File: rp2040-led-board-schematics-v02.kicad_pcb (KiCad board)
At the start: 2 copper layers, 135.9 x 80 mm, 98 parts, among them IC1 UA78L05CDR, J1 GPIO, J10 LED1Terminal, J2 PWR_IN, J3 LED1Terminal, J4 LED1Terminal, J5 LED1Terminal, J6 LED1Terminal, J7 LED1Terminal, J8 LED1Terminal, J9 LED1Terminal, SW1 Button, SW2 PEC16-2115F-S0012, U1 Pico, U10 MAX485E, U2 ENC28J60, U3 MAX485E, U4 MAX485E, U5 MAX485E, U6 MAX485E, U7 MAX485E, U8 MAX485E, U9 MAX485E

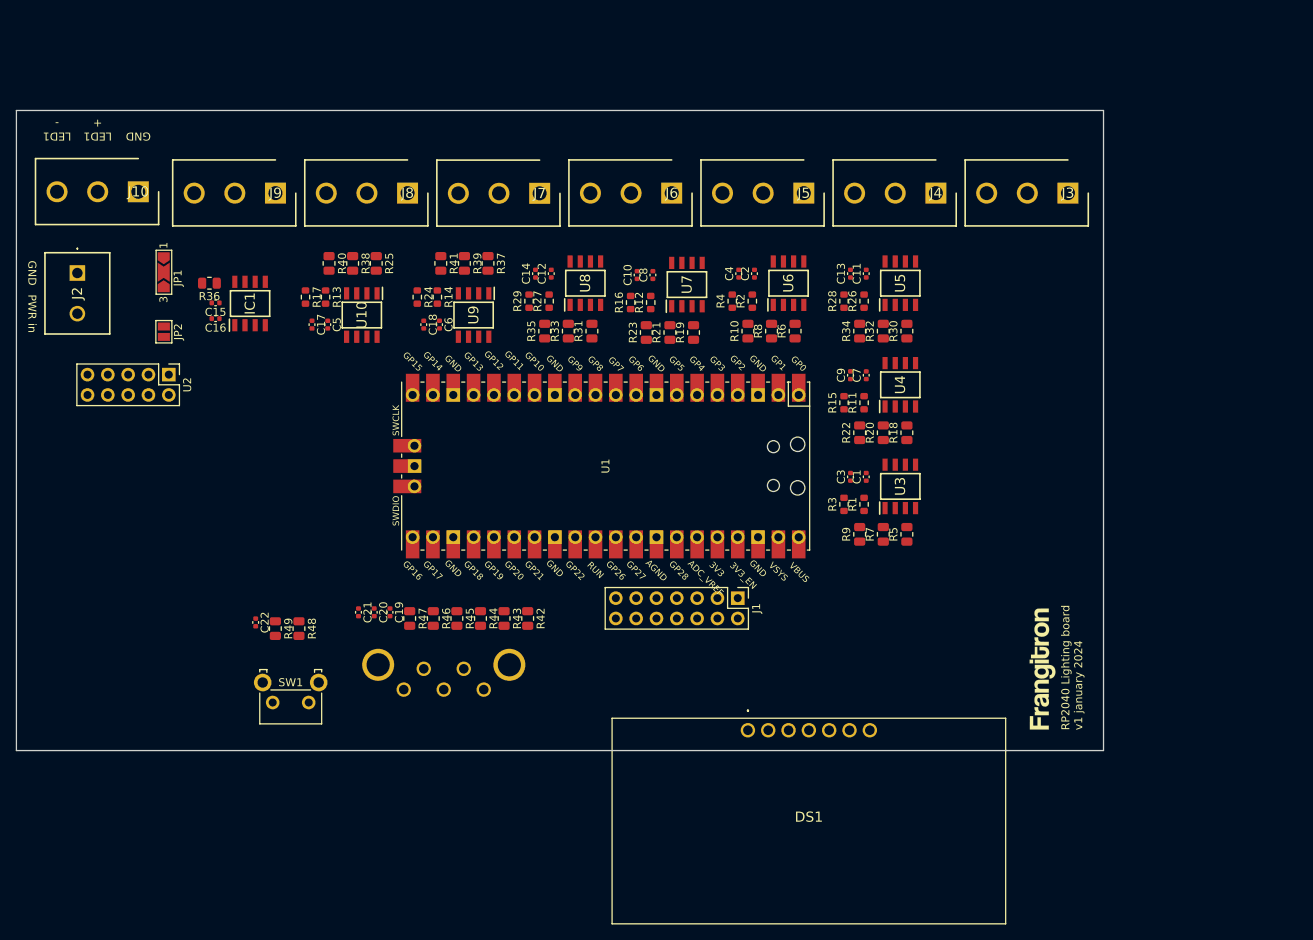
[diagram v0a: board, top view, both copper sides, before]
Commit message: footprints ok
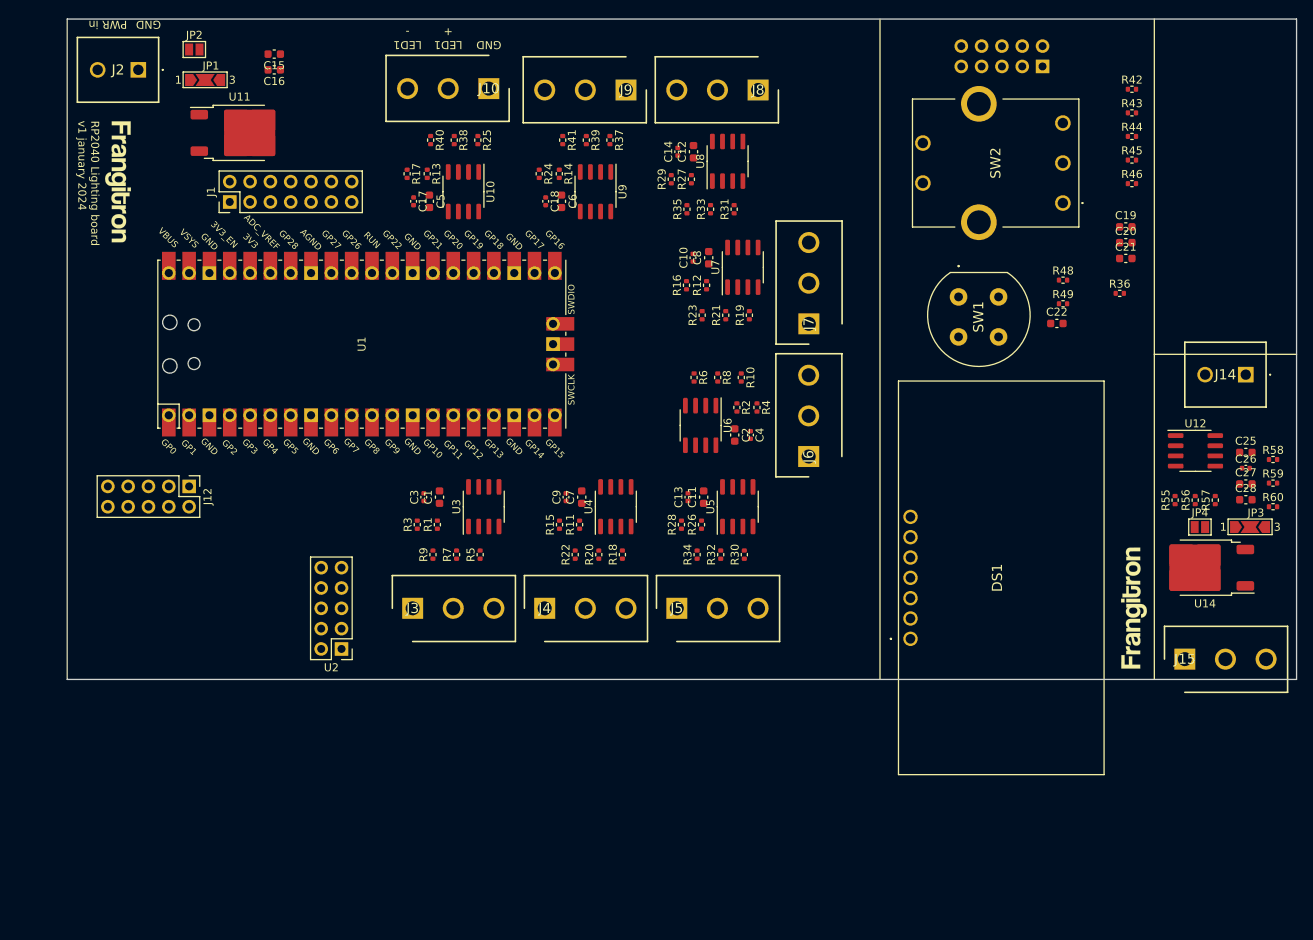
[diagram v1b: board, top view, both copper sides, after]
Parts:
- removed IC1: UA78L05CDR, SamacSys_Parts:SOIC127P600X175-8N
- removed R47: 1k, Resistor_SMD:R_0805_2012Metric
- added C25: 100nF, Capacitor_SMD:C_0603_1608Metric, F.Cu at (222.3, 98.6)
- added C26: 10uF, Capacitor_SMD:C_0402_1005Metric, F.Cu at (222.3, 100.6)
- added C27: 220nF, Capacitor_SMD:C_0603_1608Metric, F.Cu at (222.3, 102.6)
- added C28: 100nF, Capacitor_SMD:C_0603_1608Metric, F.Cu at (222.3, 104.5)
- added H2: ~, Frangitron:frangitron_logo_16mm, F.Cu at (208.3, 118.1)
- added H4: ~, Frangitron:frangitron_logo_16mm, B.Cu at (213.4, 105.4)
- added J11: MainBoard, Connector_PinHeader_2.54mm:PinHeader_2x05_P2.54mm_Vertical, B.Cu at (196.8, 50.4)
- added J12: FrontPanel, Connector_PinHeader_2.54mm:PinHeader_2x05_P2.54mm_Vertical, F.Cu at (90.2, 102.9)
- added J14: ReceiverData, Frangitron:ScrewTerminal_01x02_5.08_Amphenol, F.Cu at (222.2, 88.9)
- added J15: ReceiverRS485, Frangitron:ScrewTerminal_01x03_5.08_Amphenol, F.Cu at (214.6, 124.5)
- added JP3: 1-2 12V, Jumper:SolderJumper-3_P2.0mm_Open_TrianglePad1.0x1.5mm_NumberLabels, F.Cu at (222.8, 108.0)
- added JP4: 12V, Jumper:SolderJumper-2_P1.3mm_Open_Pad1.0x1.5mm, F.Cu at (216.5, 108.0)
- added R55: 10K, Resistor_SMD:R_0402_1005Metric, F.Cu at (213.4, 104.6)
- added R56: 10K, Resistor_SMD:R_0402_1005Metric, F.Cu at (215.9, 104.6)
- added R57: 10K, Resistor_SMD:R_0402_1005Metric, F.Cu at (218.4, 104.6)
- added R58: 20K, Resistor_SMD:R_0402_1005Metric, F.Cu at (225.7, 99.5)
- added R59: 20K, Resistor_SMD:R_0402_1005Metric, F.Cu at (225.7, 102.5)
- added R60: 120, Resistor_SMD:R_0402_1005Metric, F.Cu at (225.7, 105.4)
- added U11: LM7805, Package_TO_SOT_SMD:TO-252-2, F.Cu at (96.5, 58.7)
- added U12: MAX485E, Package_SO:SOIC-8_3.9x4.9mm_P1.27mm, F.Cu at (216.0, 98.4)
- added U14: LM7805, Package_TO_SOT_SMD:TO-252-2, F.Cu at (217.2, 113.0)
- C1, C11, C12, C19, C2, C20, C21, C22, C5, C6, C7, C8: footprint Capacitor_SMD:C_0402_1005Metric -> Capacitor_SMD:C_0603_1608Metric
- C15: value 100nF -> 220nF; footprint Capacitor_SMD:C_0402_1005Metric -> Capacitor_SMD:C_0603_1608Metric
- C16: value 10uF -> 100nF; footprint Capacitor_SMD:C_0402_1005Metric -> Capacitor_SMD:C_0603_1608Metric
- DS1: footprint SamacSys_Parts:NHD0216AWIB3 -> Frangitron:NewHaven-OLED-NHD-0216AW-IB3
- J10, J3, J4, J5, J6, J7, J8, J9: footprint SamacSys_Parts:SHDR3W110P0X508_1X3_1524X810X1015P -> Frangitron:ScrewTerminal_01x03_5.08_Amphenol
- J2: footprint SamacSys_Parts:5442206 -> Frangitron:ScrewTerminal_01x02_5.08_Amphenol
- R1, R11, R12, R13, R14, R15, R16, R17, R2, R24, R26, R27, R28, R29, R3, R4: footprint Resistor_SMD:R_0603_1608Metric -> Resistor_SMD:R_0402_1005Metric
- R10, R18, R19, R20, R21, R22, R23, R25, R30, R31, R32, R33, R34, R35, R37, R38, R39, R40, R41, R42, R43, R44, R45, R46, R48, R49, R5, R6, R7, R8, R9: footprint Resistor_SMD:R_0805_2012Metric -> Resistor_SMD:R_0402_1005Metric
- R36: value 120 -> 1k; footprint Resistor_SMD:R_0805_2012Metric -> Resistor_SMD:R_0402_1005Metric
- SW1: footprint Button_Switch_THT:SW_Tactile_SKHH_Angled -> Frangitron:C&K_PushButtonSwitch_SPST_D6C90F2LFS
- SW2: value PEC16-2115F-S0012 -> PEC16; footprint SamacSys_Parts:PEC162115FS0012 -> SamacSys_Parts:PEC164120FS0012; moved to F.Cu
- U10, U3, U4, U5, U6, U7, U8, U9: footprint SamacSys_Parts:SOIC127P600X175-8N -> Package_SO:SOIC-8_3.9x4.9mm_P1.27mm
- moved H1 130.7 mm to (81.3, 64.8), turned to -90 degrees
- moved R36 113.8 mm to (206.5, 78.7), turned to 0 degrees
- moved C22 106.9 mm to (198.6, 82.5), turned to 0 degrees
- moved R49 106.5 mm to (199.4, 80.0), turned to 0 degrees
- moved C21 105.6 mm to (207.3, 74.4), turned to 0 degrees
- moved R48 105.0 mm to (199.4, 77.1), turned to 0 degrees
- moved C20 104.7 mm to (207.3, 72.4), turned to 0 degrees
- moved C19 103.8 mm to (207.3, 70.4), turned to 0 degrees
- moved R46 102.9 mm to (208.0, 65.0), turned to 0 degrees
- moved R45 102.0 mm to (208.0, 62.1), turned to 0 degrees
- moved R44 101.3 mm to (208.0, 59.1), turned to 0 degrees
- moved R43 100.8 mm to (208.0, 56.2), turned to 0 degrees
- moved R42 100.4 mm to (208.0, 53.2), turned to 0 degrees
- moved J3 97.0 mm to (118.1, 118.1), turned to 0 degrees
- moved SW1 95.8 mm to (186.3, 79.2), turned to -90 degrees
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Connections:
- C16 pad 1: Net-(IC1-OUTPUT) -> Net-(JP2-A)
- C19 pad 1: EncoderA -> FPEncoderA
- C20 pad 1: EncoderB -> FPEncoderB
- C21 pad 1: EncoderS -> FPEncoderS
- C22 pad 1: SwitchPush -> FPSwitchPush
- DS1 pad 5: PI i2c0 SDA -> FPDisplaySCL
- DS1 pad 6: PI i2c0 SCL -> FPDisplaySDA
- DS1 pad 7: PI i2c0 RST -> FPDisplayRST
- JP2 pad 1: Net-(IC1-OUTPUT) -> Net-(JP2-A)
- R36 pad 1: Net-(IC1-OUTPUT) -> Net-(R36-Pad1)
- R36 pad 2: GND -> FPEncoderS
- R42 pad 2: EncoderA -> FPEncoderA
- R43 pad 2: EncoderB -> FPEncoderB
- R44 pad 2: EncoderS -> FPEncoderS
- R45 pad 1: EncoderA -> FPEncoderA
- R46 pad 1: EncoderB -> FPEncoderB
- R48 pad 1: SwitchPush -> FPSwitchPush
- R48 pad 2: Net-(R48-Pad2) -> Net-(SW1-K)
- R49 pad 2: SwitchPush -> FPSwitchPush
- SW1 pad 1: GND -> unconnected-(SW1-Pad1)
- SW1 pad 2: Net-(R48-Pad2) -> GND
- SW2 pad C1: Net-(SW2-COMMON) -> GND
- SW2 pad D1: GND -> Net-(R36-Pad1)
- U1 pad 1: EncoderA -> MBEncoderA
- U1 pad 19: SwitchPush -> MBSwitchPush
- U1 pad 2: EncoderB -> MBEncoderB
- U1 pad 4: EncoderS -> MBEncoderS
- U1 pad 5: PI i2c0 RST -> MBDisplayRST
- U1 pad 6: PI i2c0 SDA -> MBDisplaySDA
- U1 pad 7: PI i2c0 SCL -> MBDisplaySCL
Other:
- board size 135.9 x 80 mm -> 153.7 x 82.5 mm

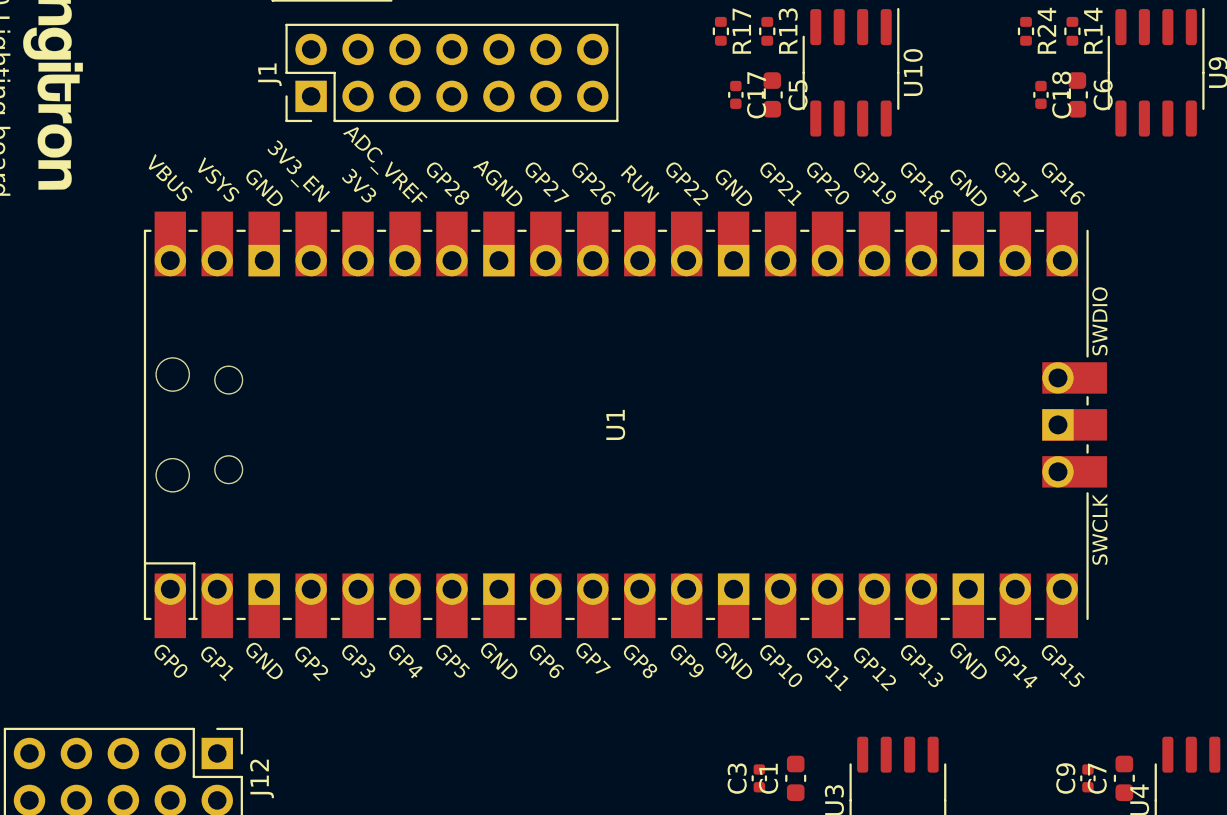
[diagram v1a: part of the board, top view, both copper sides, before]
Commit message: start Phil's Lab tutorial
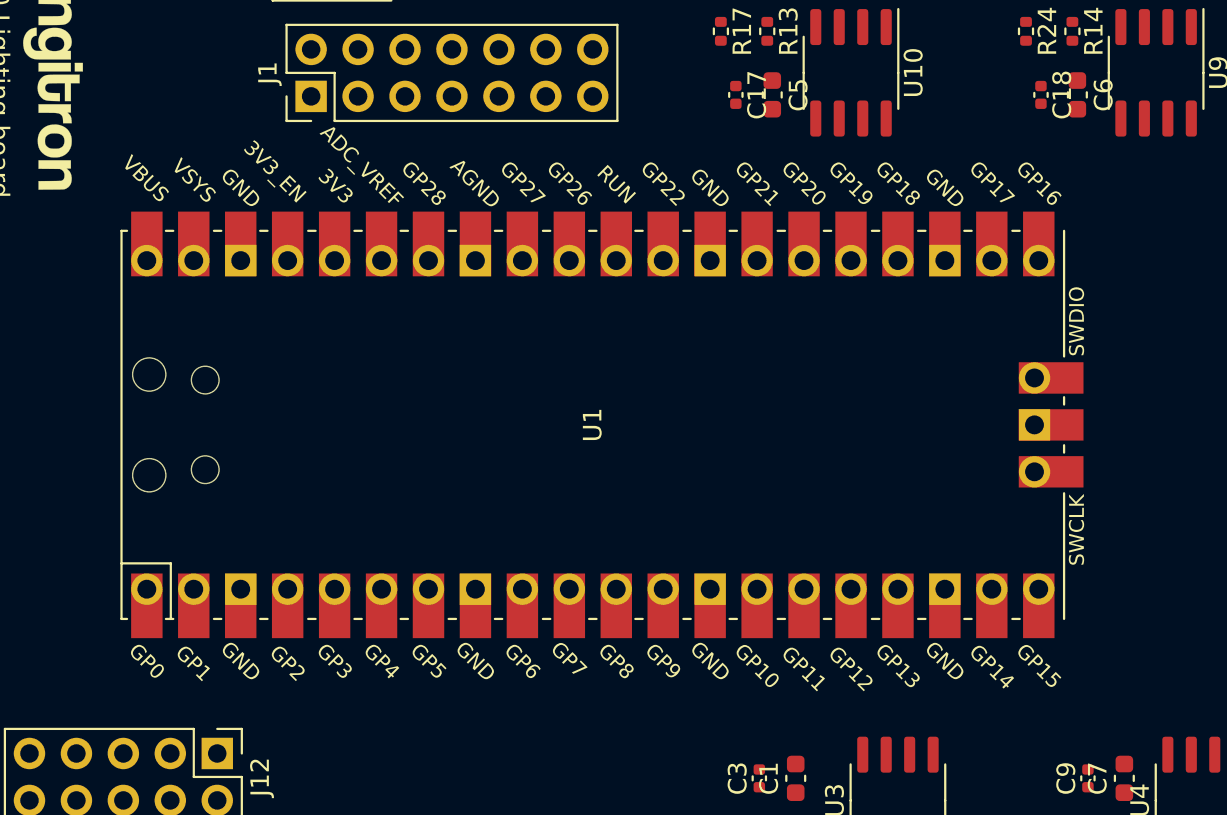
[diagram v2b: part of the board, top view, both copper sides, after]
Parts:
- moved U1 1.27 mm to (110.5, 85.1)
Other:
- copper layers 2 -> 4
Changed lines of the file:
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@@
 (kicad_pcb (version 20221018) (generator pcbnew)
   (general
-    (thickness 1.6)
+    (thickness 0.19)
   )
   (paper "A4")
   (layers
     (0 "F.Cu" signal)
+    (1 "In1.Cu" signal)
+    (2 "In2.Cu" signal)
     (31 "B.Cu" signal)
     (32 "B.Adhes" user "B.Adhesive")
-    (33 "F.Adhes" user "F.Adhesive")
     (34 "B.Paste" user)
     (35 "F.Paste" user)
@@
     (40 "Dwgs.User" user "User.Drawings")
     (41 "Cmts.User" user "User.Comments")
-    (42 "Eco1.User" user "User.Eco1")
-    (43 "Eco2.User" user "User.Eco2")
     (44 "Edge.Cuts" user)
     (45 "Margin" user)
@@
     (47 "F.CrtYd" user "F.Courtyard")
     (48 "B.Fab" user)
-    (49 "F.Fab" user)
     (50 "User.1" user)
     (51 "User.2" user)
-    (52 "User.3" user)
-    (53 "User.4" user)
-    (54 "User.5" user)
-    (55 "User.6" user)
-    (56 "User.7" user)
-    (57 "User.8" user)
-    (58 "User.9" user)
   )
   (setup
+    (stackup
+      (layer "F.SilkS" (type "Top Silk Screen"))
+      (layer "F.Paste" (type "Top Solder Paste"))
+      (layer "F.Mask" (type "Top Solder Mask") (thickness 0.01))
+      (layer "F.Cu" (type "copper") (thickness 0.035))
+      (layer "dielectric 1" (type "prepreg") (thickness 0.01) (material "FR4") (epsilon_r 4.5) (loss_tangent 0.02))
+      (layer "In1.Cu" (type "copper") (thickness 0.035))
+      (layer "dielectric 2" (type "core") (thickness 0.01) (material "FR4") (epsilon_r 4.5) (loss_tangent 0.02))
+      (layer "In2.Cu" (type "copper") (thickness 0.035))
+      (layer "dielectric 3" (type "prepreg") (thickness 0.01) (material "FR4") (epsilon_r 4.5) (loss_tangent 0.02))
+      (layer "B.Cu" (type "copper") (thickness 0.035))
+      (layer "B.Mask" (type "Bottom Solder Mask") (thickness 0.01))
+      (layer "B.Paste" (type "Bottom Solder Paste"))
+      (layer "B.SilkS" (type "Bottom Silk Screen"))
+      (copper_finish "None")
+      (dielectric_constraints no)
+    )
     (pad_to_mask_clearance 0)
     (pcbplotparams
@@
   )
   (footprint "MCU_RaspberryPi_and_Boards:RPi_Pico_SMD_TH" (layer "F.Cu")
-    (at 111.76 85.09 90)
+    (at 110.49 85.09 90)
     (descr "Through hole straight pin header, 2x20, 2.54mm pitch, double rows")
     (tags "Through hole pin header THT 2x20 2.54mm double row")
